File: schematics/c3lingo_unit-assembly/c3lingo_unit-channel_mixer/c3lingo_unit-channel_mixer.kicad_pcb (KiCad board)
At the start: 2 copper layers, 75 x 90 mm, 95 parts, among them J301 Interconnect, J303 I/O, Q301 MMBFJ113, SW301 OnAir_X, SW302 Mute_X, U301 TL072, U302 LM339, U303 LM339, U304 LM339, U305 LM833-N

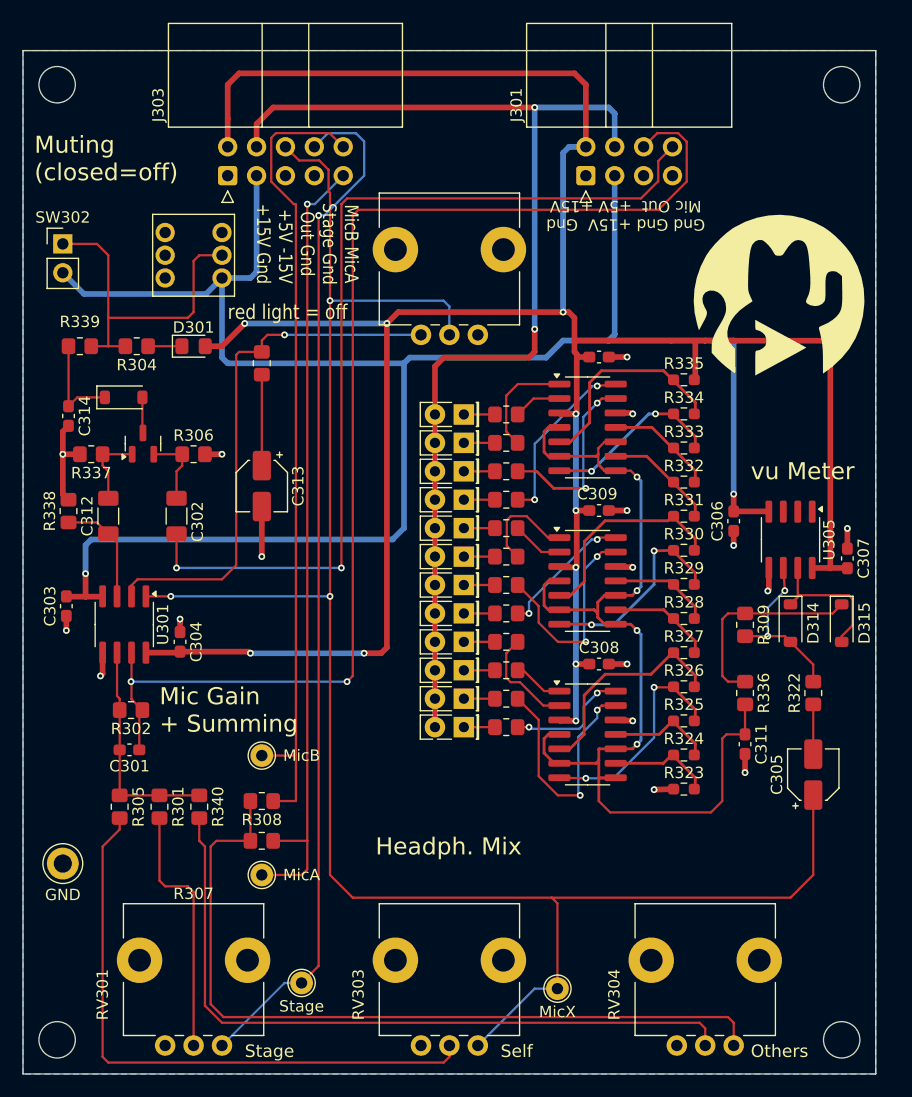
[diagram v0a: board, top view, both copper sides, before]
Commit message: Channel-Mixer: Replace mute-button connector
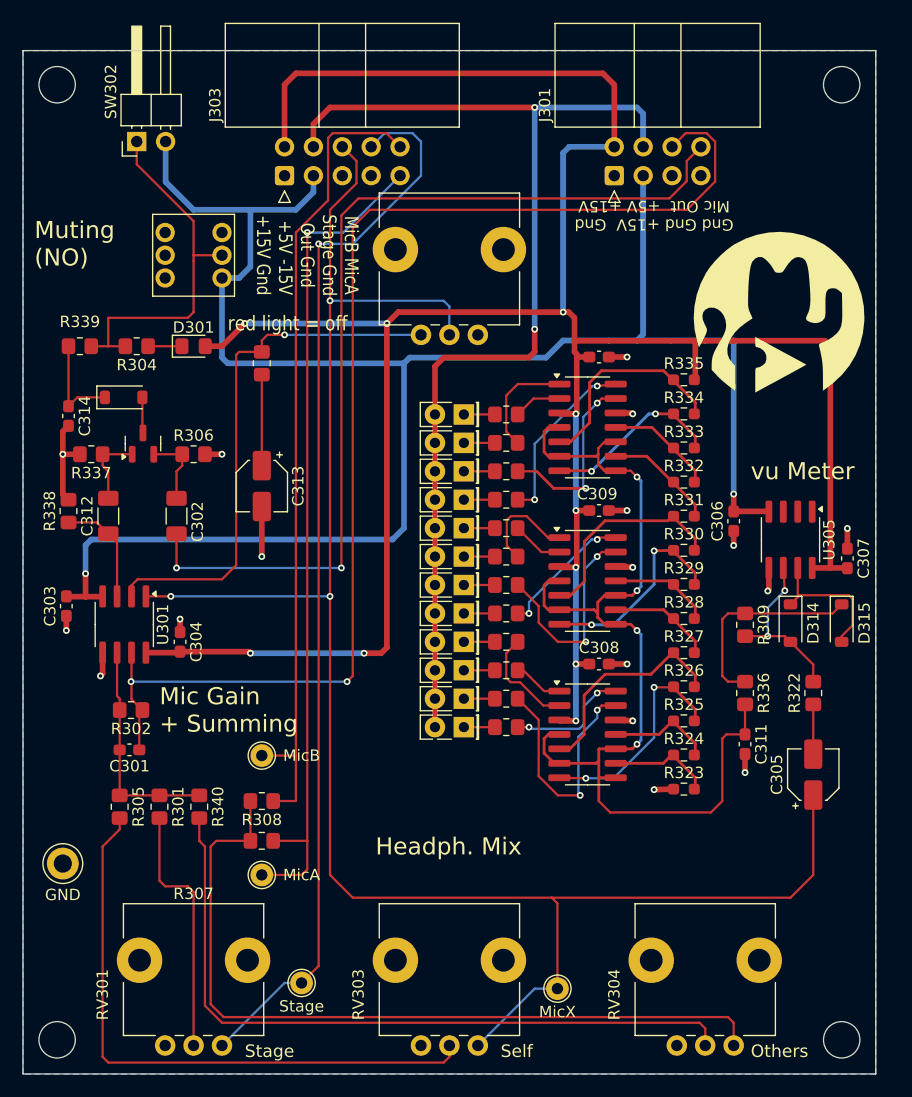
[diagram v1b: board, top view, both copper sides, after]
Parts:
- SW302: footprint Connector_PinHeader_2.54mm:PinHeader_1x02_P2.54mm_Vertical -> Connector_PinHeader_2.54mm:PinHeader_1x02_P2.54mm_Horizontal
- moved SW302 11.1 mm to (60.0, 88.0), turned to 90 degrees
- moved J303 5.00 mm to (73.0, 91.0)
- moved J301 2.50 mm to (102.0, 91.0)
- moved G*** 1.50 mm to (116.5, 103.0)
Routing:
- net /Stage: track 91.0 -> 94.6 mm
- net /Mic_OthersA: track 69.9 -> 73.4 mm
- net +5V: track 99.8 -> 97.3 mm
- net Net-(SW301A-B): track 30.3 -> 32.8 mm
- net /Headphone: track 108.0 -> 109.9 mm
- net /MicPre: track 81.7 -> 83.7 mm
- net /Mic_X: track 164.9 -> 163.7 mm
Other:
- board text added: "Muting (NO)"
- board text added: "c3lingo Interpreter Unit Channel Mixer v0.5.0-dev 2024-00-08"
- board text removed: "Muting (closed=off)"
- board text removed: "c3lingo Interpreter Unit Channel Mixer v0.4.0 2024-08-26"

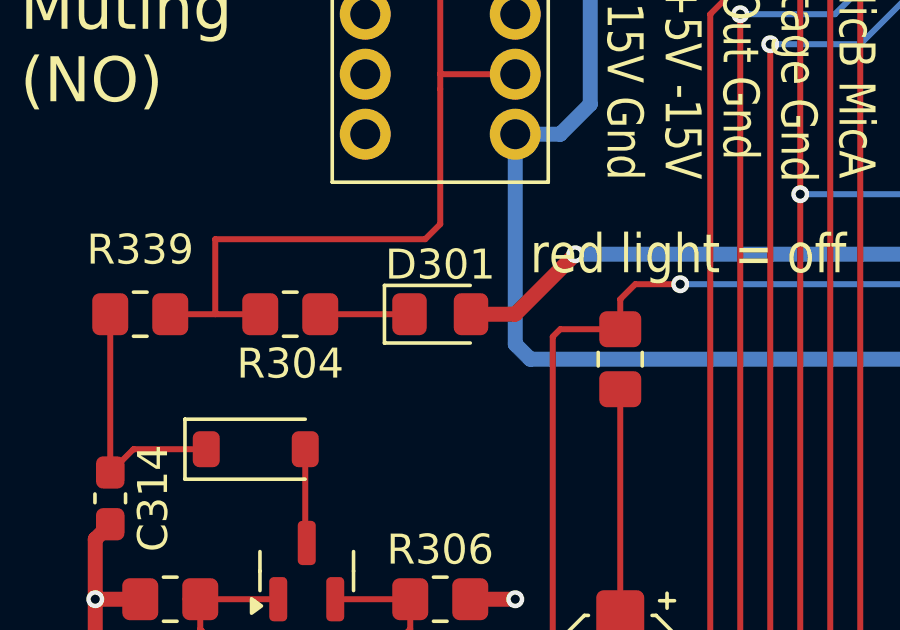
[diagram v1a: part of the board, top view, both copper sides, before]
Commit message: Channel-Mixer: Change mute LED to 3mm THD
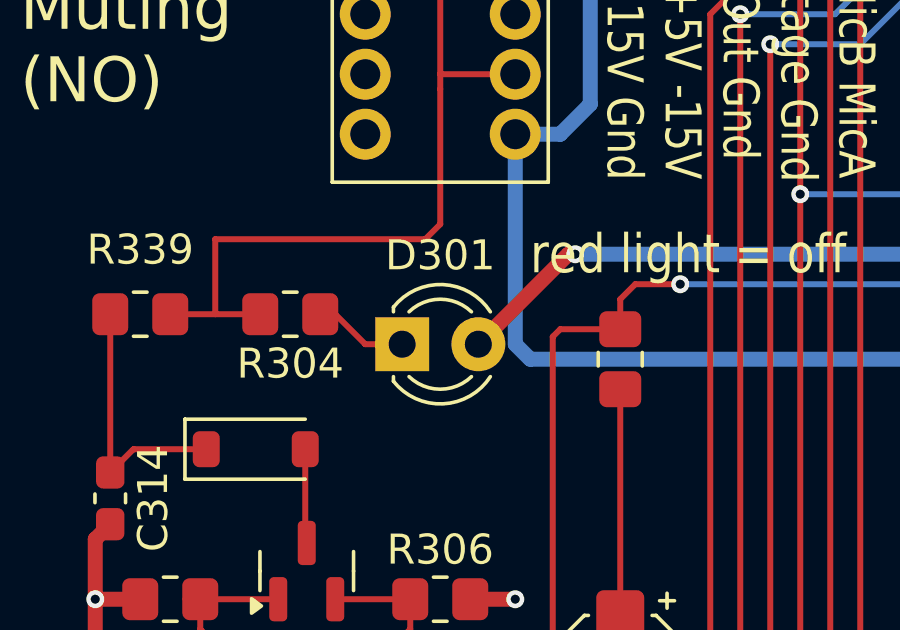
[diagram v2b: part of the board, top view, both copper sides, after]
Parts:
- D301: footprint LED_SMD:LED_0805_2012Metric_Pad1.15x1.40mm_HandSolder -> LED_THT:LED_D3.0mm
- moved D301 1.62 mm to (63.7, 107.0)
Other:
- board text added: "c3lingo Interpreter Unit Channel Mixer v0.5.0-dev 2024-09-19"
- board text removed: "c3lingo Interpreter Unit Channel Mixer v0.5.0-dev 2024-00-08"

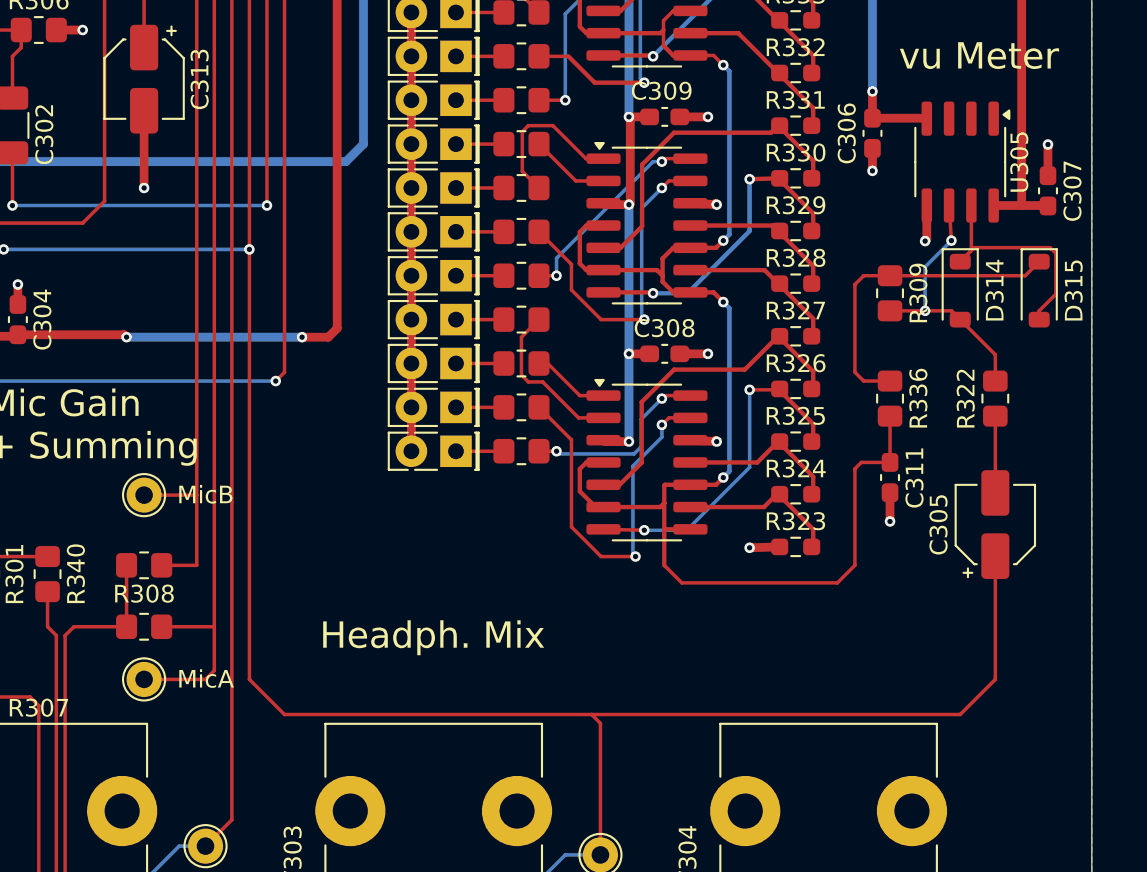
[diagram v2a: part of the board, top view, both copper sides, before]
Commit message: WIP: Add some artwork to the PCBs
TODO: OSHW
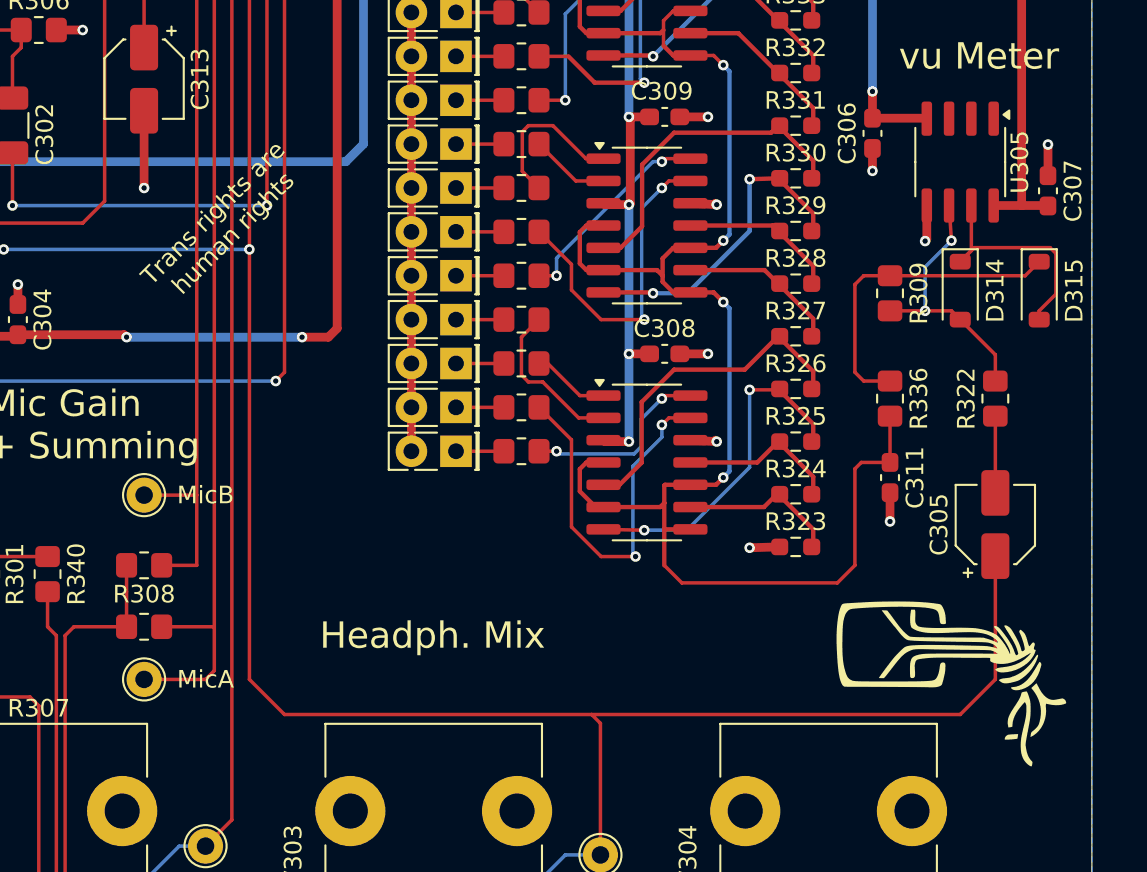
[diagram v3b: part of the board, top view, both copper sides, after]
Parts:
- added G***: LOGO, c3lingo_unit-footprints:chaosknoten-10mm, F.Cu at (117.0, 152.5)
- added G***: LOGO, c3lingo_unit-footprints:antifa-15mm, B.Cu at (108.1, 127.0)
- added G***: LOGO, c3lingo_unit-footprints:chaosknoten-15mm, B.Cu at (67.5, 127.0)
- moved G*** 32.0 mm to (87.5, 153.0)
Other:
- board text added: "Trans rights are human rights"
